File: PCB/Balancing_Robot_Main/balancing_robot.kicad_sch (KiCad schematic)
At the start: 54 parts, among them J1 Screw_Terminal_01x02, J2 USB_C_Receptacle_USB2.0, J3 Conn_01x05, J4 Conn_01x05, J5 Conn_01x05, J6 Conn_01x05, J7 Conn_01x05, J8 Conn_01x05, J9 Conn_01x05, Q1 UMH3N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

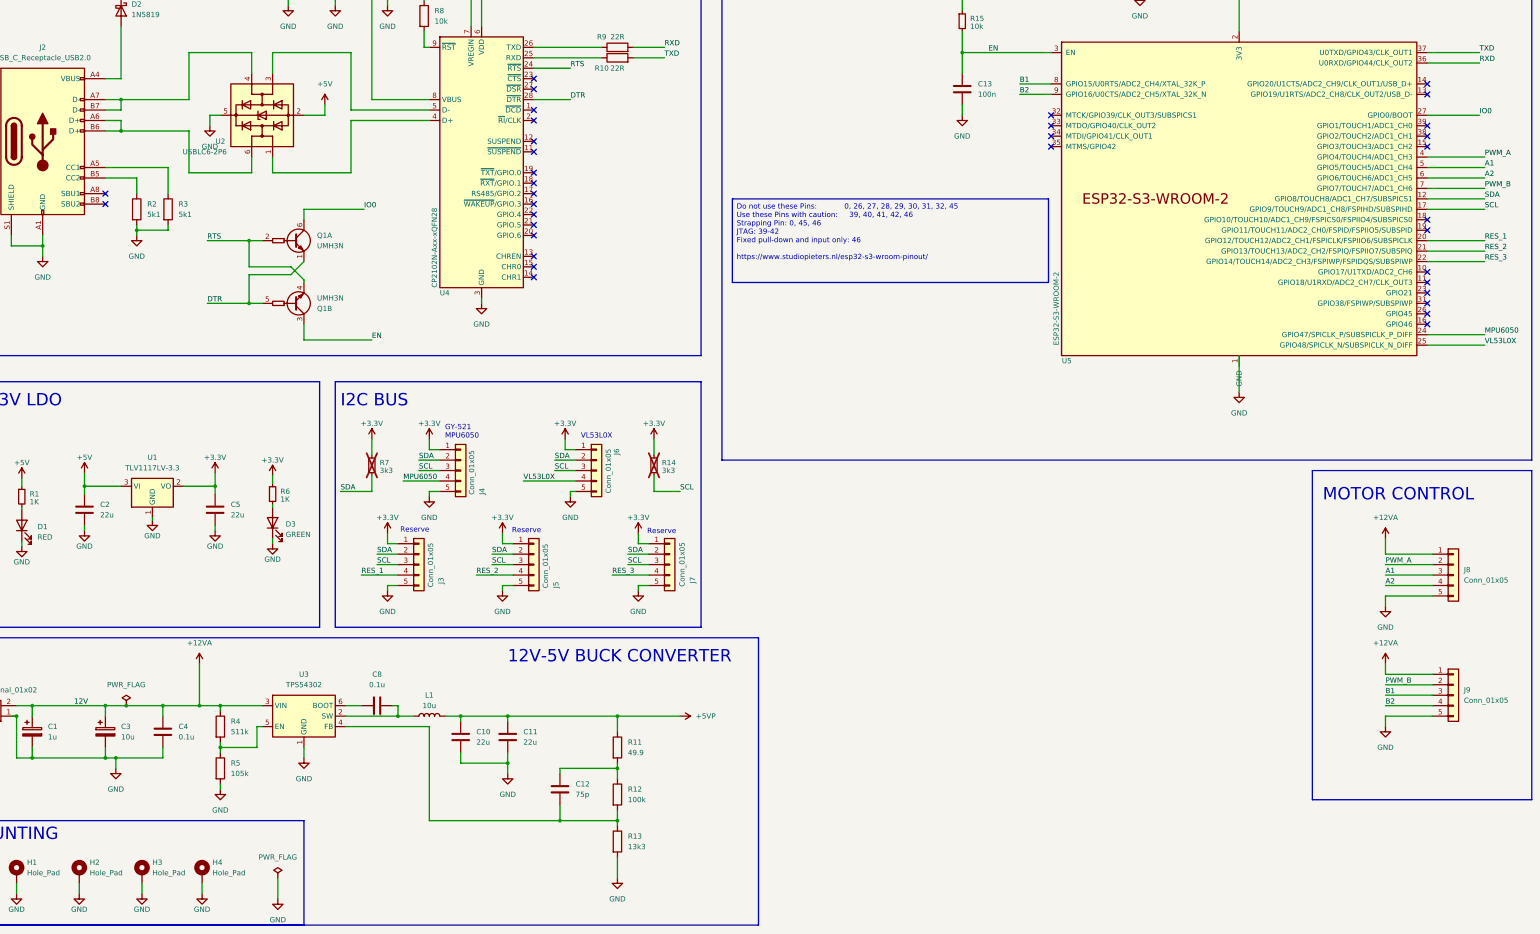
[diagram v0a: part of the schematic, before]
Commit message: Updated PCB Main and MotorBridge with Pins for Encoder
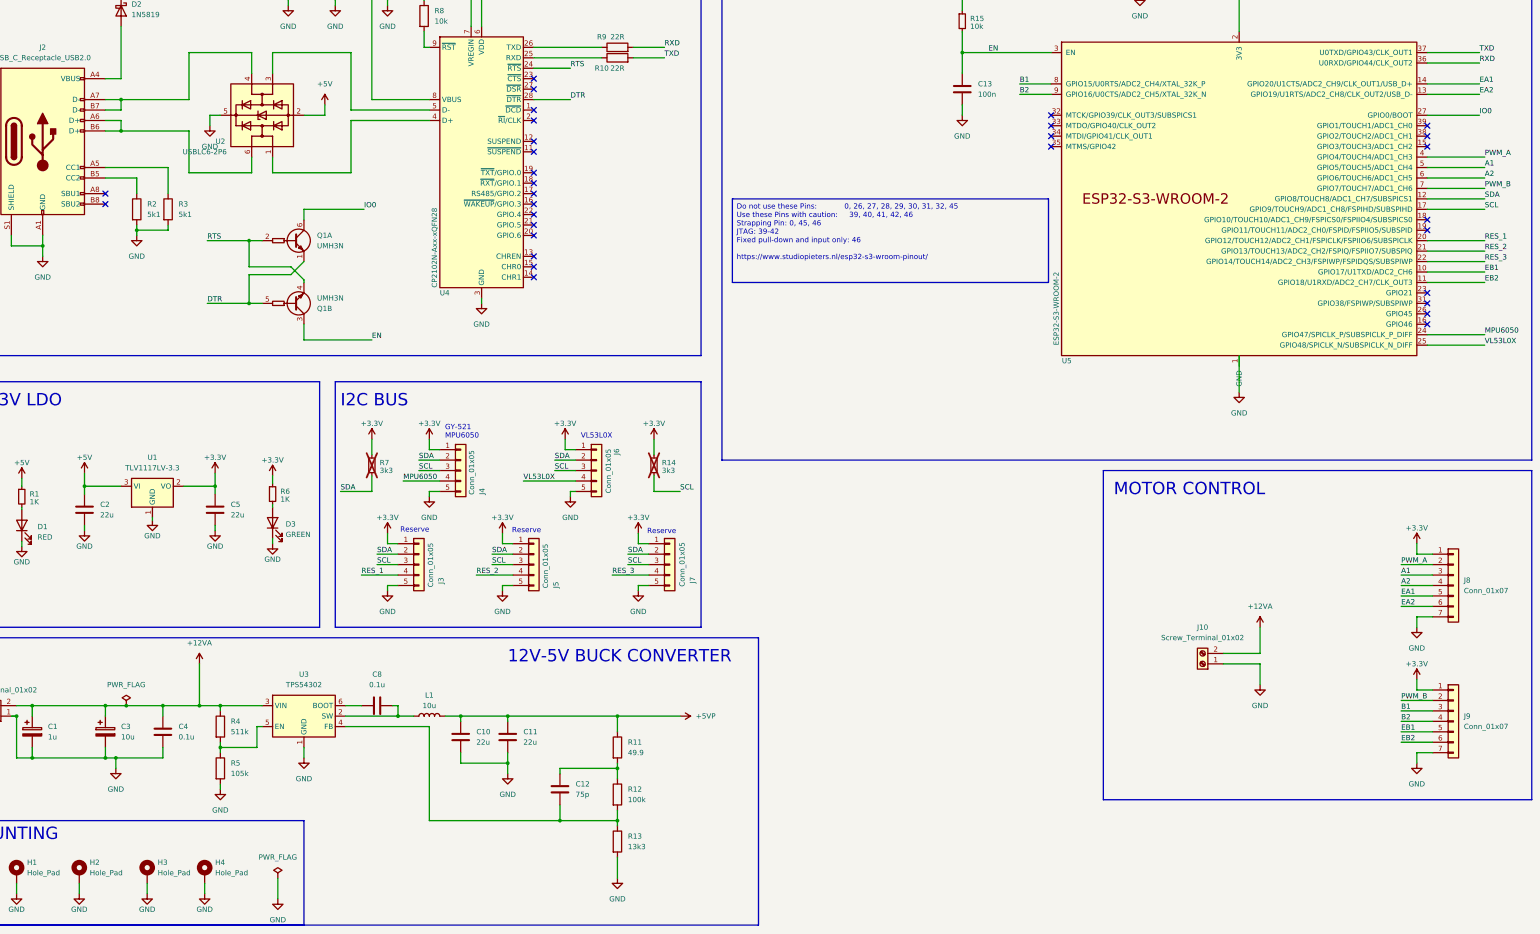
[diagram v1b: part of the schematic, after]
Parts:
- removed J8, J9: Conn_01x05, Connector_JST:JST_XH_B5B-XH-AM_1x05_P2.50mm_Vertical, symbol Connector_Generic:Conn_01x05
- added J10: Screw_Terminal_01x02, TerminalBlock_Phoenix:TerminalBlock_Phoenix_MKDS-1,5-2-5.08_1x02_P5.08mm_Horizontal, symbol Connector:Screw_Terminal_01x02
- added J8, J9: Conn_01x07, Connector_JST:JST_XH_B7B-XH-A_1x07_P2.50mm_Vertical, symbol Connector_Generic:Conn_01x07
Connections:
- net +12VA: now also J10.2 (Pin_2)
- net +3.3V: now also J8.1 (Pin_1), J9.1 (Pin_1)
- net A1: now also J8.3 (Pin_3)
- net A2: now also J8.4 (Pin_4)
- net B1: now also J9.3 (Pin_3)
- net B2: now also J9.4 (Pin_4)
- net GND: now also J10.1 (Pin_1), J8.7 (Pin_7), J9.7 (Pin_7)
- net PWM_A: now also J8.2 (Pin_2)
- net PWM_B: now also J9.2 (Pin_2)
- net EB1: now reaches U5.10 (GPIO17/U1TXD/ADC2_CH6)
- net EB1: now also J9.5 (Pin_5)
- net EB2: now reaches U5.11 (GPIO18/U1RXD/ADC2_CH7/CLK_OUT3)
- net EB2: now also J9.6 (Pin_6)
- net EA2: now reaches U5.13 (GPIO19/U1RTS/ADC2_CH8/CLK_OUT2/USB_D-)
- net EA2: now also J8.6 (Pin_6)
- net EA1: now reaches U5.14 (GPIO20/U1CTS/ADC2_CH9/CLK_OUT1/USB_D+)
- net EA1: now also J8.5 (Pin_5)
- no-connect marks 35 -> 31

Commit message: Added Visuals
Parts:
- removed R11: 49.9, Resistor_SMD:R_1206_3216Metric, symbol Device:R
- removed R4: 511k, Resistor_SMD:R_1206_3216Metric, symbol Device:R
- removed R5: 105k, Resistor_SMD:R_1206_3216Metric, symbol Device:R
- removed U3: TPS54302, Package_TO_SOT_SMD:SOT-23-6, symbol Regulator_Switching:TPS54302
- added U6: TPS62933, Package_TO_SOT_SMD:SOT-583-8, symbol Regulator_Switching:TPS62933
- C10: value 22u -> 100n
- C11: value 22u -> 47p
- C12: value 75p -> 47u
- C4: value 0.1u -> 33n
- C8: value 0.1u -> 100n
- L1: footprint Inductor_SMD:L_Bourns_SRP1245A -> Inductor_SMD:L_Bourns_SRR1208_12.7x12.7mm
- R12: value 100k -> 52k3
- R13: value 13k3 -> 10k
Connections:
- net +12VA: now also C10.2, J1.1 (Pin_1), U6.3 (VIN); no longer C4.1, J1.2 (Pin_2)
- net +5VP: now also C12.1, R12.1; no longer C10.1
- net GND: now also C10.1, C12.2, C4.1, J1.2 (Pin_2), U6.4 (GND); no longer C10.2, C11.2, C4.2, J1.1 (Pin_1)
- net SW: now reaches C8.2, L1.1
- net SW: now also U6.5 (SW)
- net at R12.2, R13.1: now also C11.2, U6.8 (FB); no longer C12.2
- net at C8.1: now also U6.6 (BST)
- new net: C4.2, U6.7 (SS)
- no-connect marks 31 -> 33
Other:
- moved on the sheet: C11, C12, C4, C8, J1, R12, R13
